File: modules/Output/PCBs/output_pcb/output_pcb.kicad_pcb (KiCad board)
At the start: 2 copper layers, 165 x 103.8 mm, 129 parts, among them J1 THONKICONN, J11 Conn_01x10_Pin, J12 Conn_01x10_Socket, J13 Conn_01x10_Pin, J2 THONKICONN, J21 Conn_01x10_Pin, J22 Conn_01x10_Socket, J23 Conn_01x10_Pin, J3 ACJS-MV-3, J4 ACJS-MV-3, J5 ACJS-MV-3, J6 Eurorack_2x5_Power, J7 Conn_01x03_Socket, U1 TL072, U10 TL074, U11 TL074, U12 TL074, U2 TL074, U3 NE5532, U4 NE5532, U5 NE5532, U6 NE5532, U7 TL074, U8 NE5532, U9 NE5532

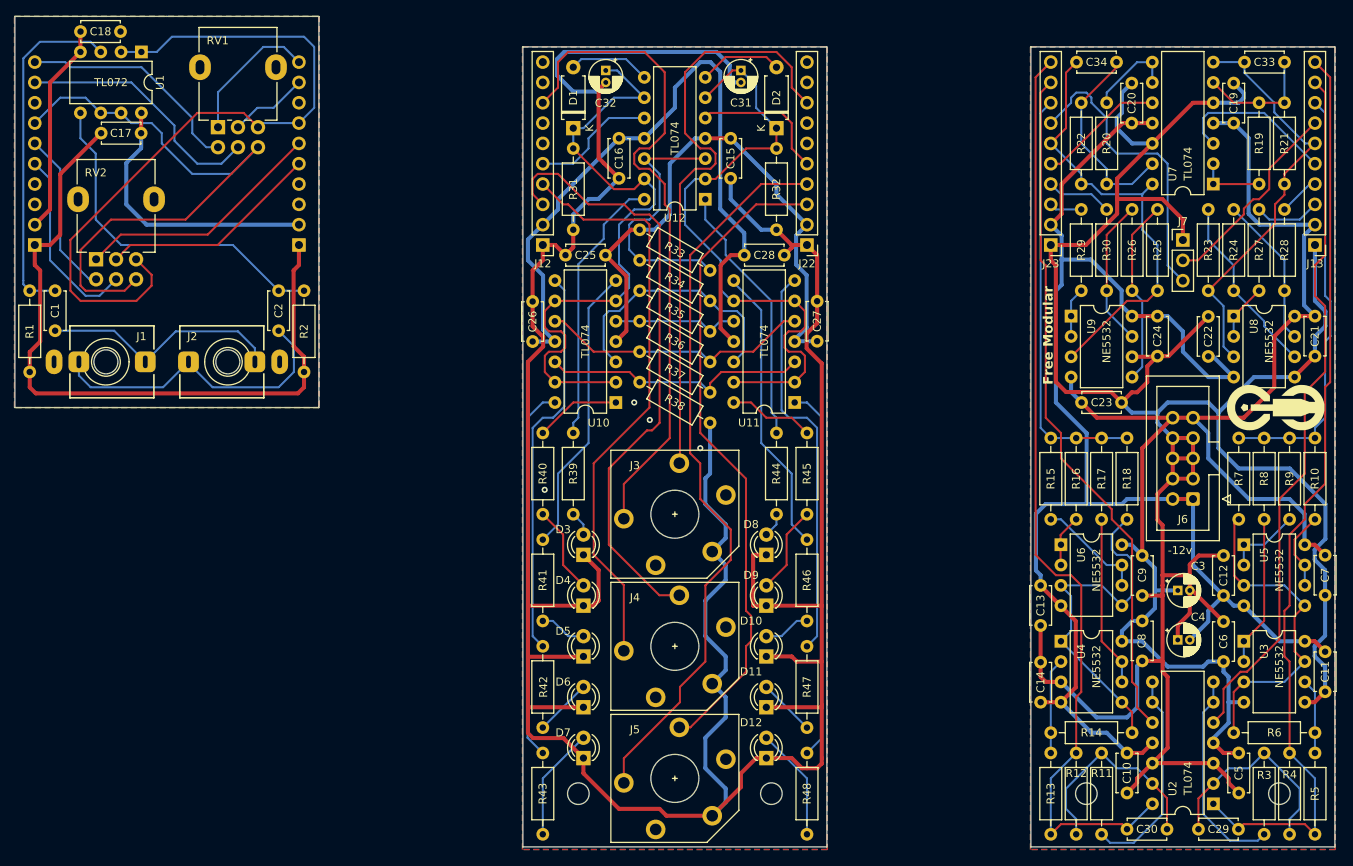
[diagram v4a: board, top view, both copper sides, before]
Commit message: fix polarity mismatch bugs in output pcb
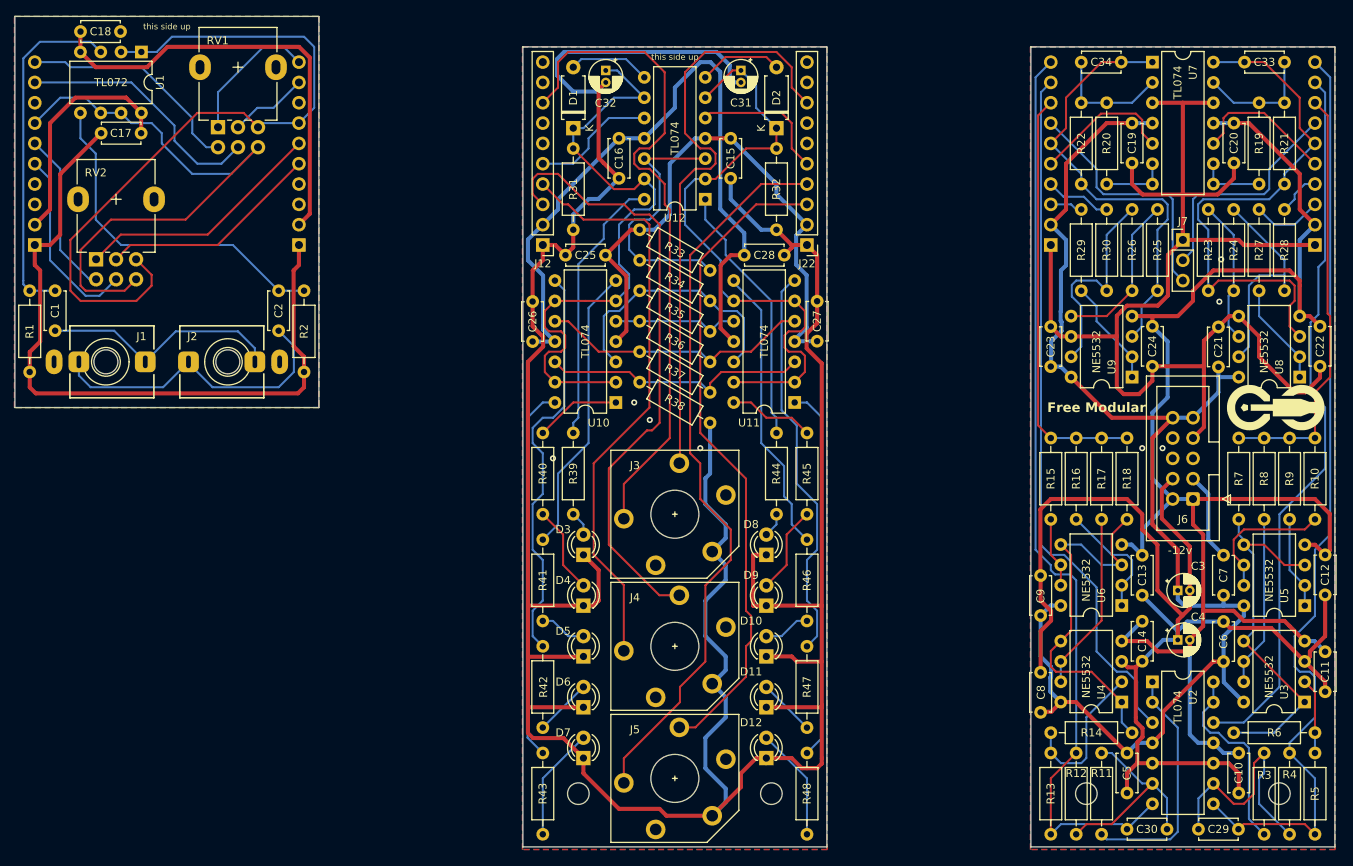
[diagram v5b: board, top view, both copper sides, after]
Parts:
- J13, J23: moved to B.Cu
- moved U2 17.0 mm to (190.5, 138.4), turned to 0 degrees
- moved U7 17.0 mm to (190.5, 61.0), turned to 0 degrees
- moved C14 16.2 mm to (189.2, 130.8), turned to -90 degrees
- moved C19 16.2 mm to (187.9, 73.6), turned to 90 degrees
- moved C22 14.5 mm to (211.5, 94.0), turned to -90 degrees
- moved C10 14.0 mm to (201.3, 147.3)
- moved C5 14.0 mm to (187.3, 152.3)
- moved C12 13.7 mm to (212.1, 122.6), turned to -90 degrees
- moved C7 13.6 mm to (199.4, 122.6), turned to -90 degrees
- moved C13 13.3 mm to (189.2, 122.6)
- moved C23 13.0 mm to (177.8, 94.0), turned to -90 degrees
- moved C9 12.9 mm to (176.5, 125.1), turned to -90 degrees
- moved C8 12.8 mm to (176.5, 137.2), turned to -90 degrees
- moved C20 12.8 mm to (200.7, 68.6), turned to -90 degrees
- moved C21 12.6 mm to (198.8, 94.1), turned to -90 degrees
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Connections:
- C29 pad 1: Net-(U2A--) -> Net-(U2C--)
- C30 pad 1: Net-(U2D--) -> Net-(U2B--)
- C33 pad 1: Net-(U7B--) -> Net-(U7D--)
- C34 pad 1: Net-(U7D--) -> Net-(U7A--)
- J11 pad 2: /+12v_FRONT -> /-12v_FRONT
- J13 pad 2: /+12v_REAR -> /-12v_REAR
- J21 pad 2: /-12v_FRONT -> /+12v_FRONT
- J23 pad 2: /-12v_REAR -> /+12v_REAR
- R11 pad 1: Net-(U2C--) -> Net-(U2A--)
- R11 pad 2: Net-(U2D--) -> Net-(U2B--)
- R12 pad 1: Net-(U2D--) -> Net-(U2B--)
- R19 pad 1: Net-(U7A--) -> Net-(U7C--)
- R19 pad 2: Net-(U7B--) -> Net-(U7D--)
- R20 pad 1: Net-(U7C--) -> Net-(U7B--)
- R20 pad 2: Net-(U7D--) -> Net-(U7A--)
- R21 pad 1: Net-(U7B--) -> Net-(U7D--)
- R22 pad 1: Net-(U7D--) -> Net-(U7A--)
- R3 pad 1: Net-(U2B--) -> Net-(U2D--)
- R3 pad 2: Net-(U2A--) -> Net-(U2C--)
- R4 pad 1: Net-(U2A--) -> Net-(U2C--)
- R5 pad 2: Net-(U3B--) -> Net-(U3A--)
- R6 pad 1: Net-(U3B--) -> Net-(U3A--)
- R6 pad 2: Net-(U3A-+) -> Net-(U3B-+)
- R7 pad 1: Net-(U3A-+) -> Net-(U3B-+)
- R8 pad 1: Net-(U3A--) -> Net-(U3B--)
- U2 pad 1: /Headphone Amp/POT_L_1 -> Net-(U2A--)
- U2 pad 10: /Headphone Amp/POT_R_2 -> /GND_REAR
- U2 pad 12: /GND_REAR -> /Headphone Amp/POT_L_2
- U2 pad 14: /Headphone Amp/POT_R_1 -> Net-(U2D--)
- U2 pad 3: /GND_REAR -> /Headphone Amp/POT_R_2
- U2 pad 5: /Headphone Amp/POT_L_2 -> /GND_REAR
- U2 pad 7: Net-(U2B--) -> /Headphone Amp/POT_R_1
- U2 pad 8: Net-(U2C--) -> /Headphone Amp/POT_L_1
- U3 pad 1: Net-(U3A--) -> Net-(U3B-+)
- U3 pad 3: Net-(U3A-+) -> /GND_REAR
- U3 pad 4: /+12v_REAR -> /-12v_REAR
- U3 pad 5: /GND_REAR -> Net-(U3B-+)
- U3 pad 7: Net-(U3A-+) -> Net-(U3B--)
- U3 pad 8: /-12v_REAR -> /+12v_REAR
- U5 pad 3: Net-(U3A-+) -> Net-(U3B-+)
- U5 pad 5: Net-(U3A-+) -> Net-(U3B-+)
- U7 pad 1: Net-(U7A--) -> /Line Level Amp/POT_R_1
- U7 pad 10: /Line Level Amp/POT_R_2 -> /Line Level Amp/POT_L_2
- U7 pad 14: /Line Level Amp/POT_R_1 -> /Line Level Amp/POT_L_1
- U7 pad 3: /Line Level Amp/POT_L_2 -> /GND_REAR
- U7 pad 5: /GND_REAR -> /Line Level Amp/POT_R_2
- U7 pad 7: /Line Level Amp/POT_L_1 -> Net-(U7B--)
- U9 pad 4: /+12v_REAR -> /-12v_REAR
- U9 pad 8: /-12v_REAR -> /+12v_REAR
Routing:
- net Net-(U3B-+): track 0.00 -> 46.4 mm
- net Net-(U3A-+): track 41.2 -> 0.00 mm
- net /-12v_FRONT: track 26.5 -> 55.1 mm
- net /Line Level Amp/POT_L_1: track 51.9 -> 67.7 mm
- net /GND_REAR: track 334.3 -> 322.3 mm, vias 0 -> 4
- net Net-(U3B--): track 9.42 -> 21.4 mm
- net Net-(U7D--): track 25.1 -> 15.0 mm
- net Net-(U3A--): track 18.8 -> 9.44 mm
- net Net-(U6A--): track 6.53 -> 15.3 mm
- net /+12v_REAR: track 176.1 -> 167.6 mm
- net Net-(R24-Pad2): track 19.0 -> 27.2 mm
- net Net-(R26-Pad2): track 18.5 -> 26.6 mm
- net Net-(U5B--): track 9.83 -> 17.5 mm
- net /-12v_REAR: track 192.5 -> 199.8 mm
- net Net-(U4A--): track 12.0 -> 19.2 mm
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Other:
- board text added: "Output back v1.1"
- board text added: "Output front v1.1"
- board text added: "this side up"
- board text removed: "Output back v1.0"
- board text removed: "Output front v1.0"

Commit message: adjusted resistor values in output
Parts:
- R33: value 51kΩ -> 33kΩ
- R34: value 3k3kΩ -> 2k2Ω
- R35: value 2k4Ω -> 1k5Ω
- R36: value 3k6Ω -> 2k4Ω
- R37: value 1k3Ω -> 820Ω
- R38: value 750Ω -> 470Ω
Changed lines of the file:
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@@
 			)
 		)
-		(property "Value" "3k6Ω"
+		(property "Value" "2k4Ω"
 			(at 5.08 2.37 150)
 			(layer "F.Fab")
@@
 			)
 		)
-		(property "Value" "51kΩ"
+		(property "Value" "33kΩ"
 			(at 5.08 2.37 150)
 			(layer "F.Fab")
@@
 			)
 		)
-		(property "Value" "2k4Ω"
+		(property "Value" "1k5Ω"
 			(at 5.08 2.37 150)
 			(layer "F.Fab")
@@
 			)
 		)
-		(property "Value" "3k3kΩ"
+		(property "Value" "2k2Ω"
 			(at 5.08 2.37 150)
 			(layer "F.Fab")
@@
 			)
 		)
-		(property "Value" "750Ω"
+		(property "Value" "470Ω"
 			(at 5.08 2.37 150)
 			(layer "F.Fab")
@@
 			)
 		)
-		(property "Value" "1k3Ω"
+		(property "Value" "820Ω"
 			(at 5.08 2.37 150)
 			(layer "F.Fab")

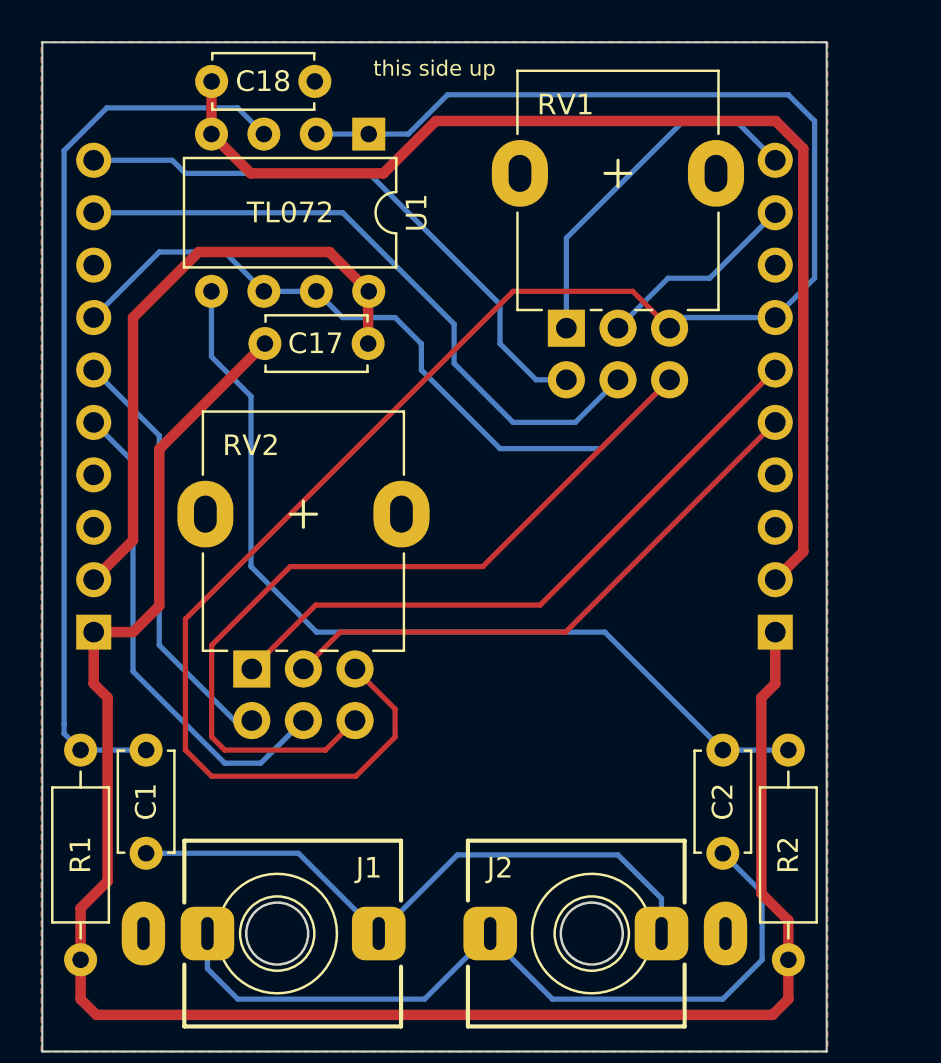
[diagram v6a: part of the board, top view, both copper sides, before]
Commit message: fix another error in output pcb
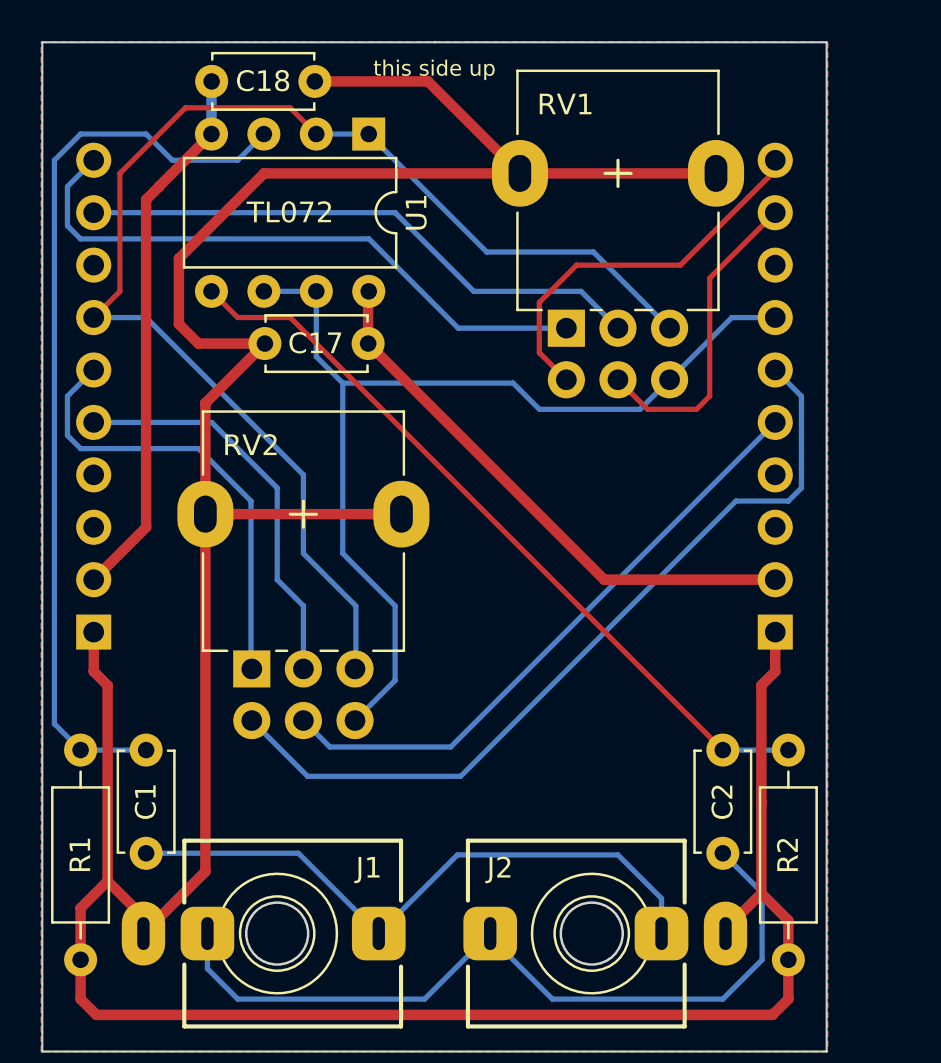
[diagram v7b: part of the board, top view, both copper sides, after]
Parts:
- moved J11 33.0 mm to (50.8, 83.8)
- moved J21 33.0 mm to (83.8, 83.8)
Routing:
- net /GND_FRONT: track 91.9 -> 167.0 mm
- net /IO Board/L_IN: track 93.8 -> 63.7 mm
- net /-12v_FRONT: track 55.1 -> 26.5 mm
- net /IO Board/R_IN: track 75.0 -> 49.0 mm
- net /IO Board/LINE_POT_R1: track 20.6 -> 39.8 mm
- net /IO Board/HP_POT_L2: track 9.94 -> 27.7 mm
- net /IO Board/HP_POT_R2: track 31.6 -> 15.5 mm
- net /IO Board/HP_POT_L1: track 17.6 -> 29.9 mm
- net /IO Board/HP_POT_R1: track 28.4 -> 18.9 mm
- net /IO Board/LINE_POT_L1: track 31.4 -> 22.1 mm
- net /IO Board/LINE_POT_L2: track 27.8 -> 19.5 mm
- net Net-(U1B-+): track 43.8 -> 37.2 mm
- net /IO Board/LINE_POT_R2: track 23.8 -> 29.9 mm
- net /+12v_FRONT: track 29.6 -> 27.0 mm
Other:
- board text added: "Output front v1.2"
- board text removed: "Output front v1.1"
